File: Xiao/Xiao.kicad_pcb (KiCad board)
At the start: 2 copper layers, 23.5 x 29.9 mm, 4 parts, among them J1 Board Connector, U1 XIAO-ESP32-S3-DIP

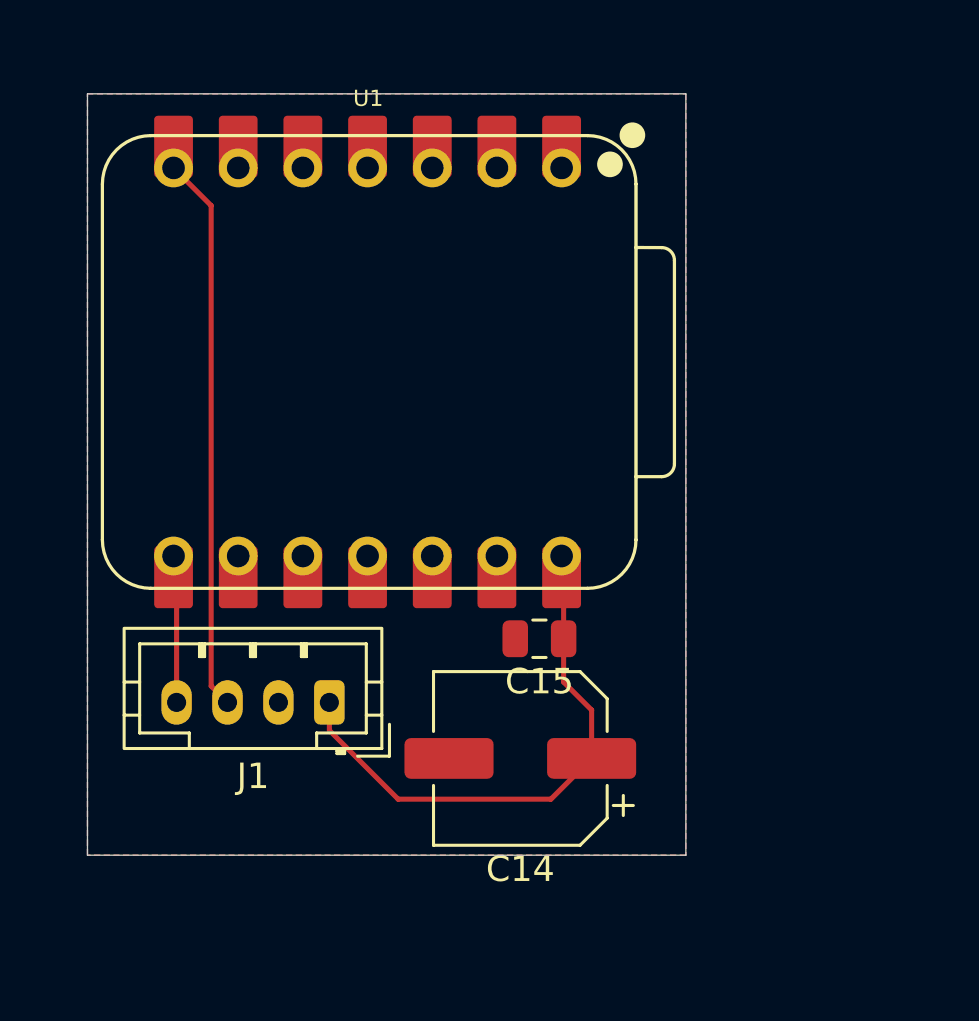
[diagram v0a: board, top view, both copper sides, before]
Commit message: Added mounting holes for the carrier
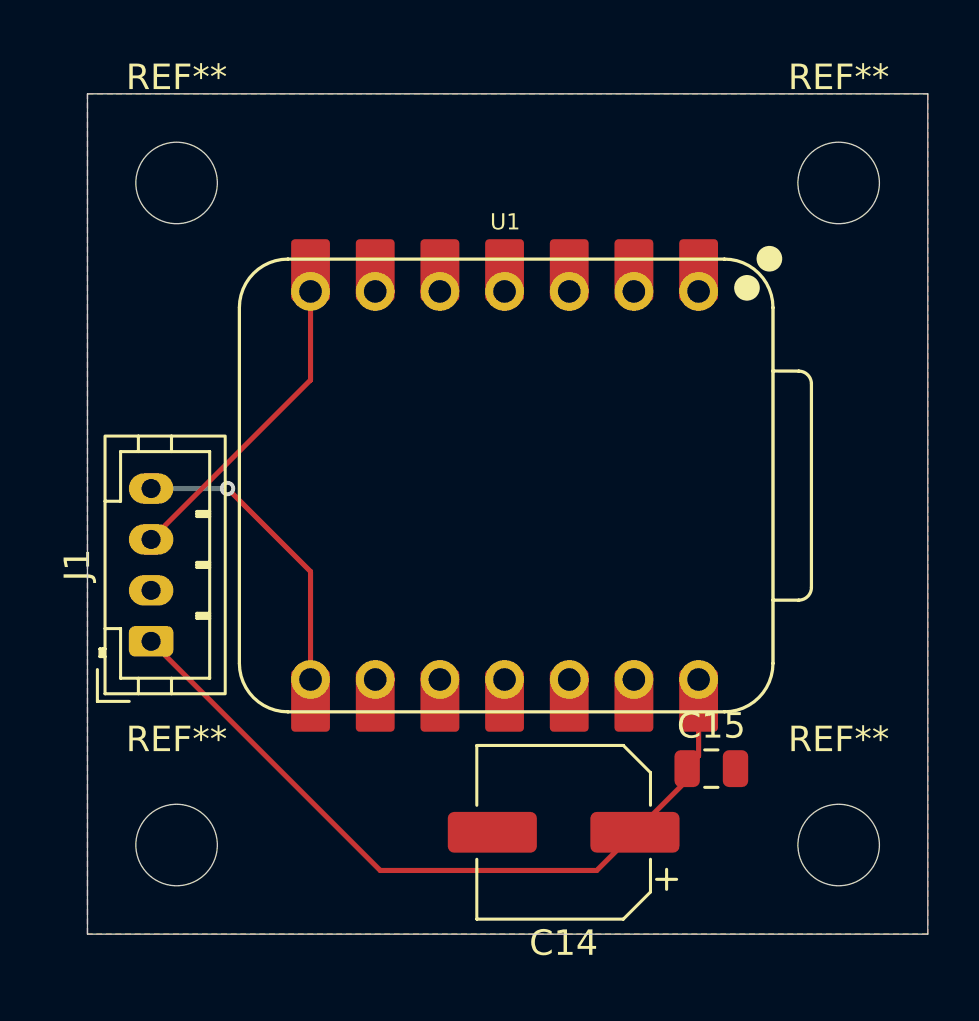
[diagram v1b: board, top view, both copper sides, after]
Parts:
- added REF**: MountingHole_3.2mm_M3, MountingHole:MountingHole_3.2mm_M3, F.Cu at (41.5, 15.5)
- added REF**: MountingHole_3.2mm_M3, MountingHole:MountingHole_3.2mm_M3, F.Cu at (41.5, 41.5)
- added REF**: MountingHole_3.2mm_M3, MountingHole:MountingHole_3.2mm_M3, F.Cu at (15.5, 15.5)
- added REF**: MountingHole_3.2mm_M3, MountingHole:MountingHole_3.2mm_M3, F.Cu at (15.5, 41.5)
- moved C15 8.46 mm to (36.5, 38.5), turned to 0 degrees
- moved J1 7.40 mm to (14.5, 33.5), turned to 90 degrees
- moved U1 7.24 mm to (28.4, 27.4)
- moved C14 3.36 mm to (30.7, 41.0)
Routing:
- net VISION_TX: track 21.9 -> 12.3 mm
- net +5V: track 21.7 -> 29.5 mm
- net VISION_RX: track 5.80 -> 11.9 mm, vias 0 -> 1
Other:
- board size 23.5 x 29.9 mm -> 33 x 33 mm

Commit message: Update net assignments and main board power
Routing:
- net VISION_RX: track 11.9 -> 10.1 mm, vias 1 -> 0
- net VISION_TX: track 12.3 -> 14.0 mm
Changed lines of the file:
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@@
 	)
 	(setup
+		(stackup
+			(layer "F.SilkS"
+				(type "Top Silk Screen")
+			)
+			(layer "F.Paste"
+				(type "Top Solder Paste")
+			)
+			(layer "F.Mask"
+				(type "Top Solder Mask")
+				(thickness 0.01)
+			)
+			(layer "F.Cu"
+				(type "copper")
+				(thickness 0.035)
+			)
+			(layer "dielectric 1"
+				(type "core")
+				(thickness 1.51)
+				(material "FR4")
+				(epsilon_r 4.5)
+				(loss_tangent 0.02)
+			)
+			(layer "B.Cu"
+				(type "copper")
+				(thickness 0.035)
+			)
+			(layer "B.Mask"
+				(type "Bottom Solder Mask")
+				(thickness 0.01)
+			)
+			(layer "B.Paste"
+				(type "Bottom Solder Paste")
+			)
+			(layer "B.SilkS"
+				(type "Bottom Silk Screen")
+			)
+			(copper_finish "None")
+			(dielectric_constraints no)
+		)
 		(pad_to_mask_clearance 0)
 		(allow_soldermask_bridges_in_footprints no)
@@
 		(capping no)
 		(filling no)
+		(zone_defaults)
 		(pcbplotparams
 			(layerselection 0x00000000_00000000_55555555_5755f5ff)
@@
 	)
 	(segment
-		(start 35.55 38.45)
-		(end 36 38)
-		(width 0.2)
+		(start 33.5 41)
+		(end 33.5 40.55)
+		(width 0.6)
 		(layer "F.Cu")
 		(net "+5V")
 	)
 	(segment
-		(start 36 38)
+		(start 35.55 36.285)
 		(end 36 35.835)
-		(width 0.2)
+		(width 0.6)
 		(layer "F.Cu")
 		(net "+5V")
 	)
 	(segment
-		(start 35.55 38.5)
-		(end 35.55 38.45)
-		(width 0.2)
-		(layer "F.Cu")
-		(net "+5V")
-	)
-	(segment
-		(start 35.55 38.95)
-		(end 35.55 38.5)
-		(width 0.2)
+		(start 32 42.5)
+		(end 33.5 41)
+		(width 0.6)
 		(layer "F.Cu")
 		(net "+5V")
@@
 		(start 14.5 33.5)
 		(end 23.5 42.5)
-		(width 0.2)
+		(width 0.6)
 		(layer "F.Cu")
 		(net "+5V")
 	)
 	(segment
-		(start 33.5 41)
-		(end 35.55 38.95)
-		(width 0.2)
-		(layer "F.Cu")
-		(net "+5V")
-	)
-	(segment
-		(start 32 42.5)
-		(end 33.5 41)
-		(width 0.2)
+		(start 33.5 40.55)
+		(end 35.55 38.5)
+		(width 0.6)
 		(layer "F.Cu")
 		(net "+5V")
@@
 		(start 23.5 42.5)
 		(end 32 42.5)
-		(width 0.2)
+		(width 0.6)
 		(layer "F.Cu")
 		(net "+5V")
 	)
 	(segment
-		(start 20.76 19.76)
-		(end 20.76 23.24)
-		(width 0.2)
+		(start 35.55 38.5)
+		(end 35.55 36.285)
+		(width 0.6)
+		(layer "F.Cu")
+		(net "+5V")
+	)
+	(segment
+		(start 19.68237 19.76)
+		(end 20.76 19.76)
+		(width 0.25)
 		(layer "F.Cu")
 		(net "VISION_TX")
 	)
 	(segment
-		(start 20.76 23.24)
-		(end 14.5 29.5)
-		(width 0.2)
+		(start 13.3 28.3)
+		(end 13.3 26.14237)
+		(width 0.25)
 		(layer "F.Cu")
 		(net "VISION_TX")
 	)
 	(segment
-		(start 20.76 30.76)
-		(end 17.5 27.5)
-		(width 0.2)
+		(start 13.3 26.14237)
+		(end 19.68237 19.76)
+		(width 0.25)
+		(layer "F.Cu")
+		(net "VISION_TX")
+	)
+	(segment
+		(start 14.5 29.5)
+		(end 13.3 28.3)
+		(width 0.25)
+		(layer "F.Cu")
+		(net "VISION_TX")
+	)
+	(segment
+		(start 14.5 27.5)
+		(end 20.76 33.76)
+		(width 0.25)
 		(layer "F.Cu")
 		(net "VISION_RX")
 	)
 	(segment
-		(start 20.76 35)
-		(end 20.76 30.76)
-		(width 0.2)
+		(start 20.76 33.76)
+		(end 20.76 35)
+		(width 0.25)
 		(layer "F.Cu")
 		(net "VISION_RX")
 	)
-	(via
-		(at 17.5 27.5)
-		(size 0.6)
-		(drill 0.3)
-		(layers "F.Cu" "B.Cu")
-		(net "VISION_RX")
-	)
-	(segment
-		(start 17.5 27.5)
-		(end 14.5 27.5)
-		(width 0.2)
-		(layer "B.Cu")
-		(net "VISION_RX")
-	)
